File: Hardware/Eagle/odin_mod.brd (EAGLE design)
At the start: 21.4 x 22.8 mm, 36 parts

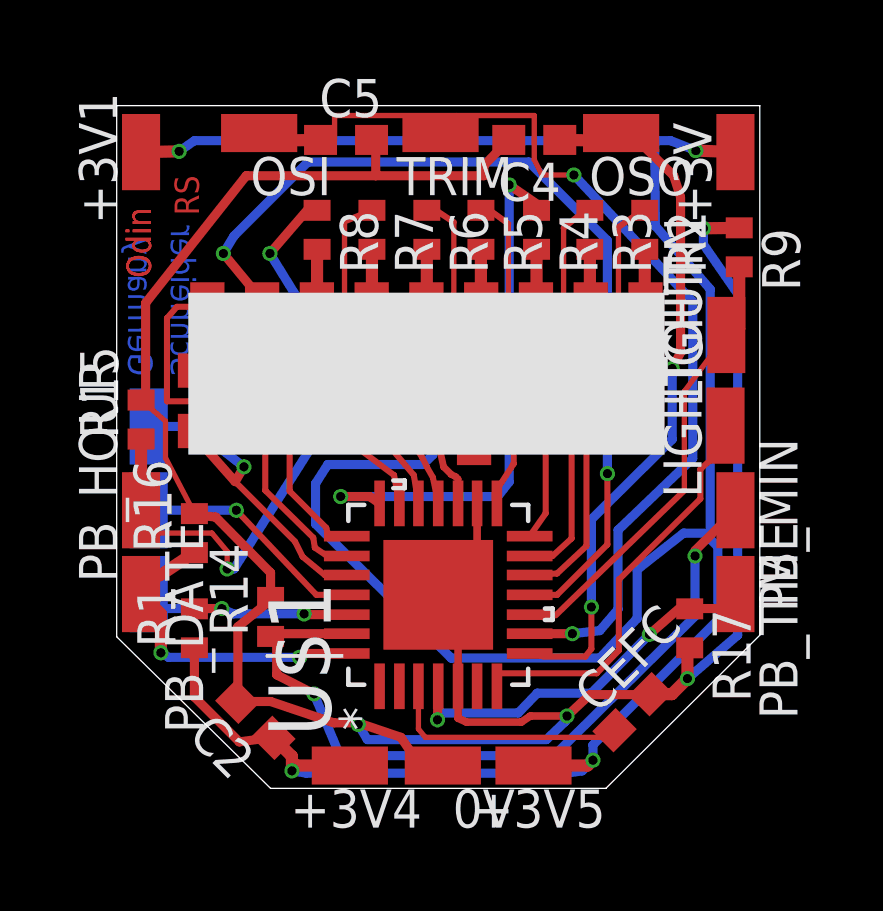
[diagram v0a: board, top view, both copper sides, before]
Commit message: Optimized Odin and Loki layout.
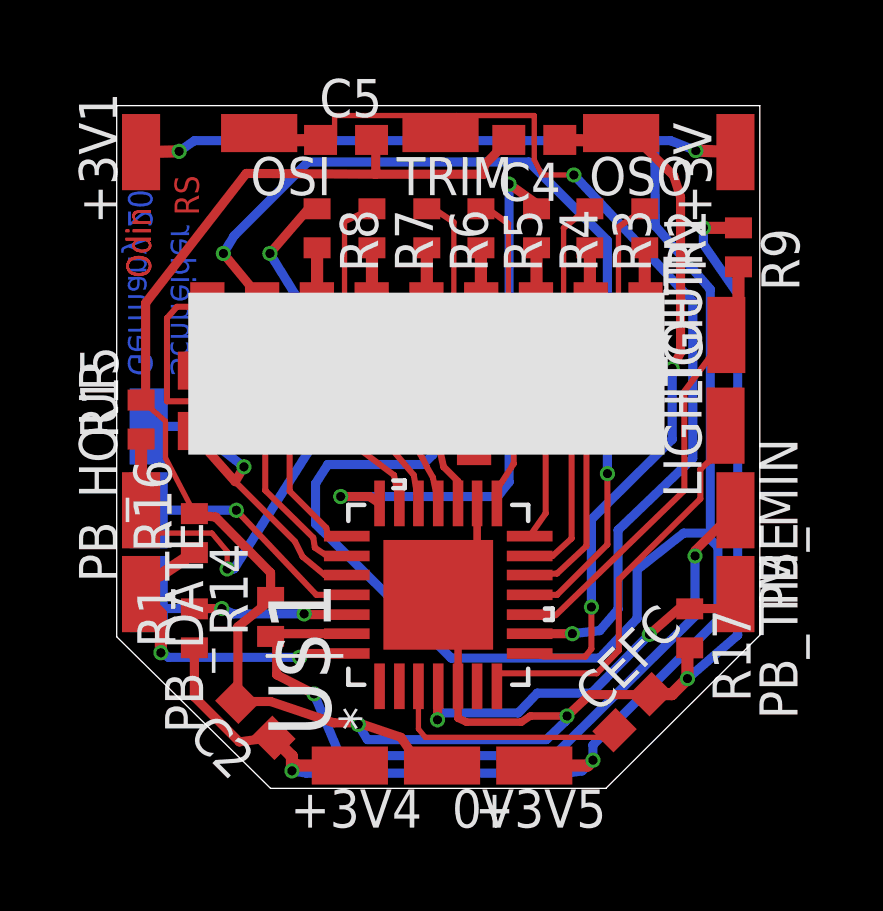
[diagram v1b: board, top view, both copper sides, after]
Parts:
- moved R2 0.05 mm to (17.6, 18.7)
- moved R3 0.05 mm to (15.7, 18.7)
- moved R4 0.05 mm to (13.9, 18.7)
- moved R5 0.05 mm to (12.1, 18.7)
- moved R6 0.05 mm to (10.3, 18.7)
- moved R7 0.05 mm to (8.46, 18.7)
- moved R8 0.05 mm to (6.63, 18.7)
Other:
- board text added: "Roy Schneider Germany 2021"
- board text removed: "Roy Schneider Germany"

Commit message: Reviewed boards and code.
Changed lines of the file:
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@@
 <plain>
 <wire x1="5.08" y1="0" x2="16.256" y2="0" width="0" layer="20"/>
-<wire x1="-0.0508" y1="5.0546" x2="5.08" y2="0" width="0" layer="20"/>
+<wire x1="-0.0508" y1="5.1054" x2="5.08" y2="0" width="0" layer="20"/>
 <wire x1="16.256" y1="0" x2="21.3868" y2="5.1054" width="0" layer="20"/>
 <wire x1="21.3868" y1="5.1054" x2="21.3868" y2="22.7584" width="0" layer="20"/>
@@
 Schneider
 Germany 2021</text>
-<wire x1="-0.0508" y1="22.7584" x2="-0.0508" y2="5.0546" width="0" layer="20"/>
+<wire x1="-0.0508" y1="22.7584" x2="-0.0508" y2="5.1054" width="0" layer="20"/>
 </plain>
 <attributes>
@@
 <wire x1="8.5852" y1="21.5646" x2="8.5852" y2="20.4724" width="0.3048" layer="1"/>
 <wire x1="8.5852" y1="20.4724" x2="12.192" y2="20.4724" width="0.3048" layer="1"/>
-<wire x1="12.192" y1="20.4724" x2="12.192" y2="20.7636" width="0.3048" layer="1"/>
-<wire x1="12.192" y1="20.7636" x2="13.0184" y2="21.6154" width="0.3048" layer="1"/>
+<wire x1="12.192" y1="20.4724" x2="12.5984" y2="20.8398" width="0.3048" layer="1"/>
+<wire x1="12.5984" y1="20.8398" x2="13.0184" y2="21.6154" width="0.3048" layer="1"/>
 <contactref element="R9" pad="1"/>
 <wire x1="20.4216" y1="18.669" x2="20.701" y2="18.669" width="0.1524" layer="1"/>
@@
 <wire x1="18.9738" y1="4.6078" x2="19.05" y2="4.684" width="0.4064" layer="1"/>
 <wire x1="19.5072" y1="18.684" x2="20.6756" y2="18.684" width="0.4064" layer="1"/>
-<wire x1="2.54" y1="9.1694" x2="1.5748" y2="11.0236" width="0.1778" layer="1"/>
 <wire x1="1.5748" y1="11.0236" x2="1.5748" y2="12.2428" width="0.1778" layer="1"/>
 <wire x1="1.5748" y1="12.2428" x2="0.762" y2="12.9436" width="0.1778" layer="1"/>
@@
 <wire x1="11.3284" y1="2.3368" x2="11.6078" y2="2.2098" width="0.254" layer="1"/>
 <wire x1="11.6078" y1="2.2098" x2="13.4366" y2="2.2098" width="0.254" layer="1"/>
+<wire x1="1.5748" y1="11.0236" x2="1.8542" y2="10.7188" width="0.1778" layer="1"/>
+<wire x1="1.8542" y1="10.7188" x2="2.54" y2="10.033" width="0.1778" layer="1"/>
+<wire x1="2.54" y1="10.033" x2="2.54" y2="9.159" width="0.1778" layer="1"/>
 </signal>
 <signal name="MCLR">
@@
 <wire x1="5.08" y1="5.1562" x2="5.08" y2="5.065" width="0.1524" layer="1"/>
 <wire x1="5.2832" y1="3.7846" x2="5.2832" y2="5.0038" width="0.3048" layer="1"/>
-<wire x1="6.5278" y1="3.1496" x2="5.2832" y2="3.7846" width="0.3048" layer="1"/>
-<wire x1="7.3914" y1="1.0922" x2="6.5278" y2="3.1496" width="0.3048" layer="16"/>
-<wire x1="14.5288" y1="1.0922" x2="7.3914" y2="1.0922" width="0.3048" layer="16"/>
-<wire x1="19.2278" y1="5.7404" x2="14.5288" y2="1.0922" width="0.3048" layer="16"/>
+<wire x1="6.6802" y1="3.2766" x2="5.2832" y2="3.7846" width="0.3048" layer="1"/>
+<wire x1="7.3914" y1="1.0668" x2="6.6802" y2="3.2766" width="0.3048" layer="16"/>
+<wire x1="14.5288" y1="1.0668" x2="7.3914" y2="1.0668" width="0.3048" layer="16"/>
+<wire x1="19.2278" y1="5.7404" x2="14.5288" y2="1.0668" width="0.3048" layer="16"/>
 <wire x1="19.2278" y1="7.747" x2="19.2278" y2="5.7404" width="0.3048" layer="16"/>
 <wire x1="19.2278" y1="7.9248" x2="19.2278" y2="7.747" width="0.3048" layer="1"/>
 <wire x1="20.574" y1="9.271" x2="19.2278" y2="7.9248" width="0.3048" layer="1"/>
 <wire x1="5.2832" y1="5.0038" x2="5.08" y2="5.065" width="0.1524" layer="1"/>
-<via x="6.5278" y="3.1496" extent="1-16" drill="0.3048"/>
+<via x="6.6802" y="3.2766" extent="1-16" drill="0.3048"/>
 <via x="19.2278" y="7.747" extent="1-16" drill="0.3048"/>
 </signal>
@@
 <wire x1="15.8242" y1="0.9398" x2="15.4686" y2="0.5842" width="0.3048" layer="16"/>
 <wire x1="19.7358" y1="8.4836" x2="19.7358" y2="16.637" width="0.3048" layer="16"/>
-<wire x1="19.304" y1="21.209" x2="19.2532" y2="21.2598" width="0.1524" layer="16"/>
 <wire x1="19.7358" y1="8.4836" x2="19.6088" y2="8.4328" width="0.1524" layer="16"/>
 <via x="2.032" y="21.2344" extent="1-16" drill="0.3048"/>
-<via x="19.2532" y="21.2598" extent="1-16" drill="0.3048"/>
+<via x="19.304" y="21.209" extent="1-16" drill="0.3048"/>
 <via x="10.4902" y="12.3444" extent="1-16" drill="0.3048"/>
 <via x="15.8242" y="0.9398" extent="1-16" drill="0.3048"/>
@@
 <wire x1="5.7912" y1="0.5842" x2="5.7912" y2="1.066796875" width="0.4064" layer="1"/>
 <wire x1="5.7912" y1="1.066796875" x2="5.173040625" y2="1.68495625" width="0.4064" layer="1"/>
-<wire x1="19.2532" y1="21.2598" x2="20.574" y2="21.209" width="0.4064" layer="1"/>
+<wire x1="19.304" y1="21.209" x2="20.574" y2="21.209" width="0.4064" layer="1"/>
 <wire x1="0.762" y1="21.209" x2="2.032" y2="21.2344" width="0.4064" layer="1"/>
 <wire x1="10.4902" y1="11.1252" x2="10.16" y2="10.795" width="0.3048" layer="16"/>
@@
 <wire x1="11.0998" y1="4.3434" x2="6.5786" y2="8.8138" width="0.3048" layer="16"/>
 <wire x1="6.5786" y1="8.8138" x2="6.5786" y2="10.16" width="0.3048" layer="16"/>
-<wire x1="19.2532" y1="21.2598" x2="18.415" y2="21.59" width="0.3048" layer="16"/>
+<wire x1="19.304" y1="21.209" x2="18.415" y2="21.59" width="0.3048" layer="16"/>
 <wire x1="18.415" y1="21.59" x2="17.8816" y2="21.59" width="0.3048" layer="16"/>
 <wire x1="17.8816" y1="21.59" x2="2.54" y2="21.59" width="0.3048" layer="16"/>
@@
 <contactref element="R4" pad="1"/>
 <wire x1="14.1732" y1="19.3294" x2="13.716" y2="19.3294" width="0.1524" layer="1"/>
-<wire x1="13.0302" y1="20.1422" x2="14.1732" y2="19.3294" width="0.3048" layer="1"/>
-<wire x1="13.0302" y1="10.2108" x2="13.0302" y2="20.1422" width="0.3048" layer="16"/>
+<wire x1="13.3096" y1="20.2438" x2="14.1732" y2="19.3294" width="0.3048" layer="1"/>
 <wire x1="8.382" y1="9.7282" x2="7.4168" y2="9.7282" width="0.3048" layer="1"/>
 <wire x1="8.7122" y1="9.4996" x2="8.382" y2="9.7282" width="0.3048" layer="1"/>
 <wire x1="13.716" y1="19.3294" x2="13.9446" y2="19.319" width="0.1524" layer="1"/>
-<via x="13.0302" y="20.1422" extent="1-16" drill="0.3048"/>
+<via x="13.3096" y="20.2438" extent="1-16" drill="0.3048"/>
 <via x="7.4168" y="9.7282" extent="1-16" drill="0.3048"/>
 <wire x1="7.4168" y1="9.7282" x2="12.6492" y2="9.7282" width="0.3048" layer="16"/>
-<wire x1="12.6492" y1="9.7282" x2="13.0302" y2="10.2108" width="0.3048" layer="16"/>
+<wire x1="13.0048" y1="10.2108" x2="13.0048" y2="19.939" width="0.3048" layer="16"/>
+<wire x1="13.0048" y1="19.939" x2="13.3096" y2="20.2438" width="0.3048" layer="16"/>
+<wire x1="12.6492" y1="9.7282" x2="13.0048" y2="10.2108" width="0.3048" layer="16"/>
 </signal>
 <signal name="RB4/LED_H4">
@@
 <contactref element="U$3" pad="P$11_KATHODE_10_HOUR"/>
 <wire x1="2.921" y1="11.3284" x2="2.81305" y2="11.9126" width="0.1524" layer="1"/>
-<wire x1="5.8928" y1="8.2296" x2="3.8989" y2="10.2235" width="0.2032" layer="1"/>
-<wire x1="3.8989" y1="10.2235" x2="2.921" y2="11.3284" width="0.3048" layer="1"/>
-<wire x1="6.1468" y1="7.7216" x2="5.8928" y2="8.2296" width="0.2032" layer="1"/>
-<wire x1="6.8834" y1="7.112" x2="6.1468" y2="7.7216" width="0.2032" layer="1"/>
+<wire x1="5.8928" y1="8.2296" x2="3.8989" y2="10.2235" width="0.2286" layer="1"/>
+<wire x1="3.8989" y1="10.2235" x2="2.921" y2="11.3284" width="0.254" layer="1"/>
+<wire x1="6.1468" y1="7.7216" x2="5.8928" y2="8.2296" width="0.2286" layer="1"/>
+<wire x1="6.8834" y1="7.112" x2="6.1468" y2="7.7216" width="0.2286" layer="1"/>
 <wire x1="7.62" y1="7.112" x2="6.8834" y2="7.112" width="0.2032" layer="1"/>
 <wire x1="2.4638" y1="12.065" x2="1.016" y2="12.065" width="0.3048" layer="16"/>
 <wire x1="4.191" y1="10.7188" x2="2.4638" y2="12.065" width="0.3048" layer="16"/>
-<wire x1="3.8989" y1="10.2235" x2="4.191" y2="10.7188" width="0.3048" layer="1"/>
+<wire x1="3.8989" y1="10.2235" x2="4.191" y2="10.7188" width="0.254" layer="1"/>
 <via x="4.191" y="10.7188" extent="1-16" drill="0.3048"/>
 </signal>

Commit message: Reviewed Odin module.
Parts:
- moved LIGHTOUT 0.18 mm to (20.2, 12.3)
- moved LIGHTIN 0.13 mm to (20.2, 15.2)
- moved C4 0.13 mm to (14.0, 21.6)
- moved C5 0.13 mm to (7.47, 21.6)
- moved OSI 0.13 mm to (4.57, 21.8)
- moved OSO 0.13 mm to (16.9, 21.8)
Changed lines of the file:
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@@
 <element name="R14" library="resistor" package="R0402" value="4.7k" x="5.08" y="5.715" rot="R90"/>
 <element name="R15" library="resistor" package="R0402" value="4.7k" x="0.762" y="12.2936" rot="R90"/>
-<element name="C4" library="resistor" package="C0603" value="12 pF" x="13.8684" y="21.6154" rot="R180"/>
-<element name="C5" library="resistor" package="C0603" value="12 pF" x="7.5946" y="21.6154"/>
+<element name="C4" library="resistor" package="C0603" value="12 pF" x="13.9954" y="21.6154" rot="R180"/>
+<element name="C5" library="resistor" package="C0603" value="12 pF" x="7.4676" y="21.6154"/>
 <element name="U$3" library="pulsar_p3_display" package="PULSAR_P3_LED_DISPLAY" value="PULSAR_P3_DISPLAY" x="2.3368" y="11.1252"/>
 <element name="+3V" library="wirepad" package="SMD1,27-2,54" value="2" x="20.574" y="21.209"/>
@@
 <element name="PAD2" library="wirepad" package="SMD1,27-2,54" value="1" x="1.016" y="9.271" rot="MR0"/>
 <element name="PAD5" library="wirepad" package="SMD1,27-2,54" value="1" x="1.016" y="6.477" rot="MR0"/>
-<element name="OSI" library="wirepad" package="SMD1,27-2,54" value="1" x="4.699" y="21.844" rot="R90"/>
-<element name="OSO" library="wirepad" package="SMD1,27-2,54" value="1" x="16.764" y="21.844" rot="R90"/>
+<element name="OSI" library="wirepad" package="SMD1,27-2,54" value="1" x="4.572" y="21.844" rot="R90"/>
+<element name="OSO" library="wirepad" package="SMD1,27-2,54" value="1" x="16.891" y="21.844" rot="R90"/>
 <element name="+3V4" library="wirepad" package="SMD1,27-2,54" value="1" x="7.7216" y="0.762" rot="R90"/>
 <element name="+3V5" library="wirepad" package="SMD1,27-2,54" value="1" x="13.8684" y="0.762" rot="R90"/>
-<element name="LIGHTIN" library="wirepad" package="SMD1,27-2,54" value="1" x="20.2692" y="15.113"/>
-<element name="LIGHTOUT" library="wirepad" package="SMD1,27-2,54" value="1" x="20.2438" y="12.0904"/>
+<element name="LIGHTIN" library="wirepad" package="SMD1,27-2,54" value="1" x="20.2438" y="15.24"/>
+<element name="LIGHTOUT" library="wirepad" package="SMD1,27-2,54" value="1" x="20.2438" y="12.2682"/>
 <element name="TRIM" library="wirepad" package="SMD1,27-2,54" value="1" x="10.7442" y="21.844" rot="R90"/>
 <element name="R9" library="resistor" package="R0402" value="47k" x="20.6756" y="18.034" rot="R270"/>
@@
 <wire x1="4.2672" y1="20.4978" x2="8.5852" y2="20.4724" width="0.3048" layer="1"/>
 <wire x1="0.9144" y1="13.0302" x2="0.9144" y2="16.1798" width="0.3048" layer="1"/>
-<wire x1="8.7884" y1="21.5646" x2="8.4446" y2="21.6154" width="0.1524" layer="1"/>
+<wire x1="8.7884" y1="21.5646" x2="8.3176" y2="21.6154" width="0.1524" layer="1"/>
 <wire x1="0.9144" y1="13.0302" x2="0.762" y2="12.9436" width="0.1524" layer="1"/>
 <wire x1="3.2512" y1="9.0424" x2="5.08" y2="7.1882" width="0.3048" layer="1"/>
@@
 <wire x1="2.5908" y1="9.1186" x2="2.54" y2="9.159" width="0.1524" layer="1"/>
 <wire x1="10.0584" y1="0.762" x2="10.795" y2="0.762" width="0.3048" layer="1"/>
-<wire x1="9.4234" y1="1.7018" x2="10.0584" y2="0.762" width="0.3048" layer="1"/>
+<wire x1="9.271" y1="1.8288" x2="10.0584" y2="0.762" width="0.3048" layer="1"/>
 <wire x1="7.1882" y1="2.1844" x2="8.001" y2="2.1844" width="0.3048" layer="1"/>
-<wire x1="8.001" y1="2.1844" x2="9.4234" y2="1.7018" width="0.3048" layer="1"/>
+<wire x1="8.001" y1="2.1844" x2="9.271" y2="1.8288" width="0.3048" layer="1"/>
 <wire x1="5.08" y1="2.8956" x2="7.1882" y2="2.1844" width="0.3048" layer="1"/>
 <wire x1="4.064" y1="2.8956" x2="5.08" y2="2.8956" width="0.3048" layer="1"/>
@@
 <wire x1="8.5852" y1="20.4724" x2="12.192" y2="20.4724" width="0.3048" layer="1"/>
 <wire x1="12.192" y1="20.4724" x2="12.5984" y2="20.8398" width="0.3048" layer="1"/>
-<wire x1="12.5984" y1="20.8398" x2="13.0184" y2="21.6154" width="0.3048" layer="1"/>
+<wire x1="12.5984" y1="20.8398" x2="13.1454" y2="21.6154" width="0.3048" layer="1"/>
 <contactref element="R9" pad="1"/>
 <wire x1="20.4216" y1="18.669" x2="20.701" y2="18.669" width="0.1524" layer="1"/>
@@
 <contactref element="C4" pad="1"/>
 <contactref element="OSO" pad="1"/>
-<wire x1="16.764" y1="21.844" x2="16.51" y2="21.59" width="0.1524" layer="1"/>
+<wire x1="16.891" y1="21.844" x2="16.51" y2="21.59" width="0.1524" layer="1"/>
 <wire x1="15.7734" y1="4.6482" x2="15.5702" y2="4.3942" width="0.2032" layer="1"/>
 <wire x1="15.7734" y1="6.0452" x2="15.7734" y2="4.6482" width="0.2032" layer="1"/>
@@
 <wire x1="18.4658" y1="13.9954" x2="18.4658" y2="11.6332" width="0.3048" layer="16"/>
 <wire x1="16.8148" y1="22.098" x2="18.5166" y2="20.4216" width="0.3048" layer="1"/>
-<wire x1="16.8148" y1="22.098" x2="16.764" y2="21.844" width="0.1524" layer="1"/>
+<wire x1="16.8148" y1="22.098" x2="16.891" y2="21.844" width="0.1524" layer="1"/>
 <via x="15.7734" y="6.0452" extent="1-16" drill="0.3048"/>
 <via x="18.4658" y="13.9954" extent="1-16" drill="0.3048"/>
 <wire x1="15.5702" y1="4.3942" x2="14.1732" y2="4.3942" width="0.2032" layer="1"/>
 <wire x1="14.1732" y1="4.3942" x2="13.716" y2="4.4958" width="0.1778" layer="1"/>
-<wire x1="16.51" y1="21.59" x2="14.7184" y2="21.6154" width="0.4064" layer="1"/>
+<wire x1="16.51" y1="21.59" x2="14.8454" y2="21.6154" width="0.4064" layer="1"/>
 <wire x1="18.4658" y1="13.9954" x2="18.7452" y2="14.5288" width="0.3048" layer="1"/>
 <wire x1="18.7452" y1="14.5288" x2="18.7452" y2="19.7104" width="0.3048" layer="1"/>
@@
 <contactref element="C5" pad="1"/>
 <contactref element="OSI" pad="1"/>
-<wire x1="4.699" y1="21.844" x2="4.953" y2="21.59" width="0.1524" layer="1"/>
+<wire x1="4.572" y1="21.844" x2="4.953" y2="21.59" width="0.1524" layer="1"/>
 <wire x1="15.1384" y1="5.1562" x2="13.716" y2="5.1562" width="0.3048" layer="1"/>
 <wire x1="16.0528" y1="5.2578" x2="15.1384" y2="5.1562" width="0.3048" layer="16"/>
@@
 <wire x1="15.1892" y1="20.447" x2="19.1516" y2="16.2306" width="0.3048" layer="16"/>
 <wire x1="14.1224" y1="20.447" x2="15.1892" y2="20.447" width="0.1778" layer="1"/>
-<wire x1="13.8684" y1="20.955" x2="14.1224" y2="20.447" width="0.1778" layer="1"/>
-<wire x1="13.8684" y1="22.4282" x2="13.8684" y2="20.955" width="0.1778" layer="1"/>
-<wire x1="7.2136" y1="22.4282" x2="11.2776" y2="22.4282" width="0.1778" layer="1"/>
-<wire x1="7.2136" y1="21.6154" x2="7.2136" y2="22.4282" width="0.1778" layer="1"/>
-<wire x1="7.2136" y1="21.6154" x2="6.7446" y2="21.6154" width="0.1524" layer="1"/>
+<wire x1="13.9954" y1="20.955" x2="14.1224" y2="20.447" width="0.1778" layer="1"/>
+<wire x1="13.9954" y1="22.4282" x2="13.9954" y2="20.955" width="0.1778" layer="1"/>
+<wire x1="7.0866" y1="22.4282" x2="11.2776" y2="22.4282" width="0.1778" layer="1"/>
+<wire x1="7.0866" y1="21.6154" x2="7.0866" y2="22.4282" width="0.1778" layer="1"/>
+<wire x1="7.0866" y1="21.6154" x2="6.6176" y2="21.6154" width="0.1524" layer="1"/>
 <via x="15.1384" y="5.1562" extent="1-16" drill="0.3048"/>
 <via x="15.1892" y="20.447" extent="1-16" drill="0.3048"/>
 <contactref element="TRIM" pad="1"/>
-<wire x1="13.8684" y1="22.4282" x2="11.2776" y2="22.4282" width="0.1778" layer="1"/>
+<wire x1="13.9954" y1="22.4282" x2="11.2776" y2="22.4282" width="0.1778" layer="1"/>
 <wire x1="11.2776" y1="22.4282" x2="10.7442" y2="21.844" width="0.1524" layer="1"/>
-<wire x1="4.953" y1="21.59" x2="6.7446" y2="21.6154" width="0.4064" layer="1"/>
+<wire x1="4.953" y1="21.59" x2="6.6176" y2="21.6154" width="0.4064" layer="1"/>
 </signal>
 <signal name="RB1/LED_M6">
@@
 <wire x1="18.8722" y1="9.9314" x2="14.5796" y2="5.7658" width="0.2032" layer="1"/>
 <wire x1="18.8722" y1="13.2334" x2="18.8722" y2="9.9314" width="0.2032" layer="1"/>
-<wire x1="20.2692" y1="15.113" x2="18.8722" y2="13.2334" width="0.2032" layer="1"/>
+<wire x1="20.2438" y1="15.24" x2="18.8722" y2="13.2334" width="0.2032" layer="1"/>
 <contactref element="R9" pad="2"/>
-<wire x1="20.2692" y1="15.113" x2="20.701" y2="15.1638" width="0.1524" layer="1"/>
+<wire x1="20.2438" y1="15.24" x2="20.701" y2="15.1638" width="0.1524" layer="1"/>
 <wire x1="20.6756" y1="17.384" x2="20.6756" y2="15.3162" width="0.4064" layer="1"/>
-<wire x1="20.6756" y1="15.3162" x2="20.2692" y2="15.113" width="0.4064" layer="1"/>
+<wire x1="20.6756" y1="15.3162" x2="20.2438" y2="15.24" width="0.4064" layer="1"/>
 </signal>
 <signal name="OSC2/RA6">
@@
 <wire x1="19.4056" y1="9.652" x2="19.4056" y2="10.6426" width="0.2032" layer="1"/>
 <wire x1="19.4056" y1="10.6426" x2="20.574" y2="11.684" width="0.2032" layer="1"/>
-<wire x1="20.574" y1="11.684" x2="20.2438" y2="12.0904" width="0.1524" layer="1"/>
+<wire x1="20.574" y1="11.684" x2="20.2438" y2="12.2682" width="0.1524" layer="1"/>
 </signal>
 <signal name="RA5/SW4">
